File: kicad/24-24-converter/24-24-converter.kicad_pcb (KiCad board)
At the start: 4 copper layers, 143.5 x 76 mm, 79 parts, among them J1 Conn_01x02, J2 Conn_01x02, M1 CSD18540Q5B, M1_1 CSD18540Q5B, M2 CSD18540Q5B, M2_1 CSD18540Q5B, M3 GENERIC_MOSFET_N, M3_1 GENERIC_MOSFET_N, M4 GENERIC_MOSFET_N, U1 LM5176PWPR

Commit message: Routing Attempt #2
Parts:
- moved Ccomp2 10.6 mm to (132.0, 107.5), turned to -90 degrees
- moved Ccomp1 8.01 mm to (129.5, 107.5), turned to -90 degrees
- moved Rpg1 6.18 mm to (162.0, 102.5)
- moved D2 5.70 mm to (159.5, 102.0), turned to 90 degrees
- moved Cvcc1 5.41 mm to (164.5, 102.5)
- moved Rcsp1 5.22 mm to (156.5, 101.0)
- moved Ccomp_1 3.96 mm to (133.5, 112.0), turned to -90 degrees
- moved Ccs1 3.54 mm to (153.5, 101.0), turned to 90 degrees
- moved Css1 3.51 mm to (135.0, 107.5)
- moved Rcsg1 2.69 mm to (150.0, 101.0)
- moved Rcomp1 2.64 mm to (129.5, 112.0)
- moved Dboot2 1.22 mm to (158.7, 106.0)
- moved Dboot1 0.97 mm to (155.0, 109.5)
- moved Cboot2 0.50 mm to (153.5, 106.0)
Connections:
- M3 pad 9: (no net) -> VOUT
- M3_1 pad 9: (no net) -> VOUT
- M4 pad 9: (no net) -> /SW2
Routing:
- net GND: track 449.2 -> 361.8 mm, vias 177 -> 18
- net Net-(U1-COMP): track 33.9 -> 17.2 mm
- net Net-(Dboot1-A): track 29.9 -> 19.9 mm
- net VOUT: track 241.1 -> 234.1 mm, vias 56 -> 3
- net /CSENSE: track 55.7 -> 61.4 mm
- net Net-(D2-A): track 7.41 -> 2.95 mm
- net Net-(D2-K): track 15.9 -> 11.9 mm
- net Net-(U1-CS): track 13.2 -> 9.29 mm
- net /HDRV1: track 60.6 -> 64.5 mm
- net Net-(U1-SS): track 10.7 -> 7.02 mm
- net /LDRV2: track 40.1 -> 37.6 mm
- net Net-(U1-CSG): track 5.07 -> 6.83 mm
- net Net-(Ccomp1-Pad2): track 5.80 -> 7.34 mm
- net /SW1: track 130.0 -> 130.8 mm, vias 54 -> 3
- net /HDRV2: track 64.9 -> 64.3 mm
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- added copper zone on F.Cu, net /CSENSE
- removed copper zone on In1.Cu, net /SW1
- removed copper zone on In1.Cu, net /SW2
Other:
- board text added: "Routing Attempt #2"
- board text removed: "Routing Attempt #1"

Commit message: All new routing around U1
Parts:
- moved D3 11.0 mm to (200.0, 56.5)
- moved R2 11.0 mm to (194.0, 56.5)
- moved Css1 3.03 mm to (137.9, 106.5), turned to 180 degrees
- moved Dboot1 2.00 mm to (157.0, 109.5)
- moved Cvcc1 0.50 mm to (164.0, 102.5)
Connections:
- M3 pad 9: VOUT -> (no net)
- M3_1 pad 9: VOUT -> (no net)
- M4 pad 9: /SW2 -> (no net)
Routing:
- net VOUT: track 234.1 -> 186.5 mm
- net Net-(U1-VIN): track 38.9 -> 55.1 mm, vias 2 -> 4
- net /HDRV2: track 64.3 -> 53.7 mm, vias 5 -> 3
- net Net-(U1-BIAS): track 12.6 -> 22.9 mm
- net GND: track 361.8 -> 352.6 mm
- net /HDRV1: track 64.5 -> 70.0 mm
- net /LDRV1: track 50.6 -> 55.6 mm
- net Net-(U1-SS): track 7.02 -> 3.14 mm
- net /SW2: track 116.1 -> 119.2 mm
- net /EN: track 26.3 -> 28.5 mm, vias 2 -> 4
- net /SW1: track 130.8 -> 128.8 mm
- net Net-(Dboot1-K): track 8.91 -> 10.9 mm
- net Net-(U1-VINSNS): track 33.1 -> 32.4 mm, vias 2 -> 4

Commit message: Added Watermark
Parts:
- added G***: LOGO, LOGO, F.Cu at (191.5, 122.0)

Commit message: Routing Attempt #3
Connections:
- M3 pad 9: (no net) -> VOUT
- M3_1 pad 9: (no net) -> VOUT
- M4 pad 9: (no net) -> /SW2
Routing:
- net GND: track 352.6 -> 38.7 mm, vias 18 -> 593
- net VIN: track 200.7 -> 37.8 mm, vias 1 -> 197
- net VOUT: track 186.5 -> 56.2 mm, vias 3 -> 58
- net /SW1: track 128.8 -> 55.7 mm, vias 3 -> 75
- net /SW2: track 119.2 -> 49.7 mm, vias 3 -> 71
- net /CSENSE: track 61.4 -> 23.3 mm, vias 1 -> 17
- net /LDRV1: track 55.6 -> 60.1 mm, vias 3 -> 4
- added copper zone on B.Cu, net /CSENSE
- added copper zone on B.Cu, net /SW1
- added copper zone on B.Cu, net /SW2
- added copper zone on B.Cu, net VIN
- added copper zone on B.Cu, net VOUT
- removed copper zone on In1.Cu, net VIN
- removed copper zone on In1.Cu, net VOUT
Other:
- board text added: "Routing Attempt #3"
- board text removed: "Routing Attempt #2"

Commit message: Routing Attempt #4
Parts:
- U1: value LM5176PWPR -> PWP0028C_N
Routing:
- net GND: vias 593 -> 614
- net /SW1: vias 75 -> 77
- net /LDRV2: vias 3 -> 4
- net /LDRV1: vias 4 -> 5
- net /CSENSE: vias 17 -> 26
- removed copper zone on F.Cu, net (none)
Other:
- board text added: "Routing Attempt #4"
- board text removed: "Routing Attempt #3"

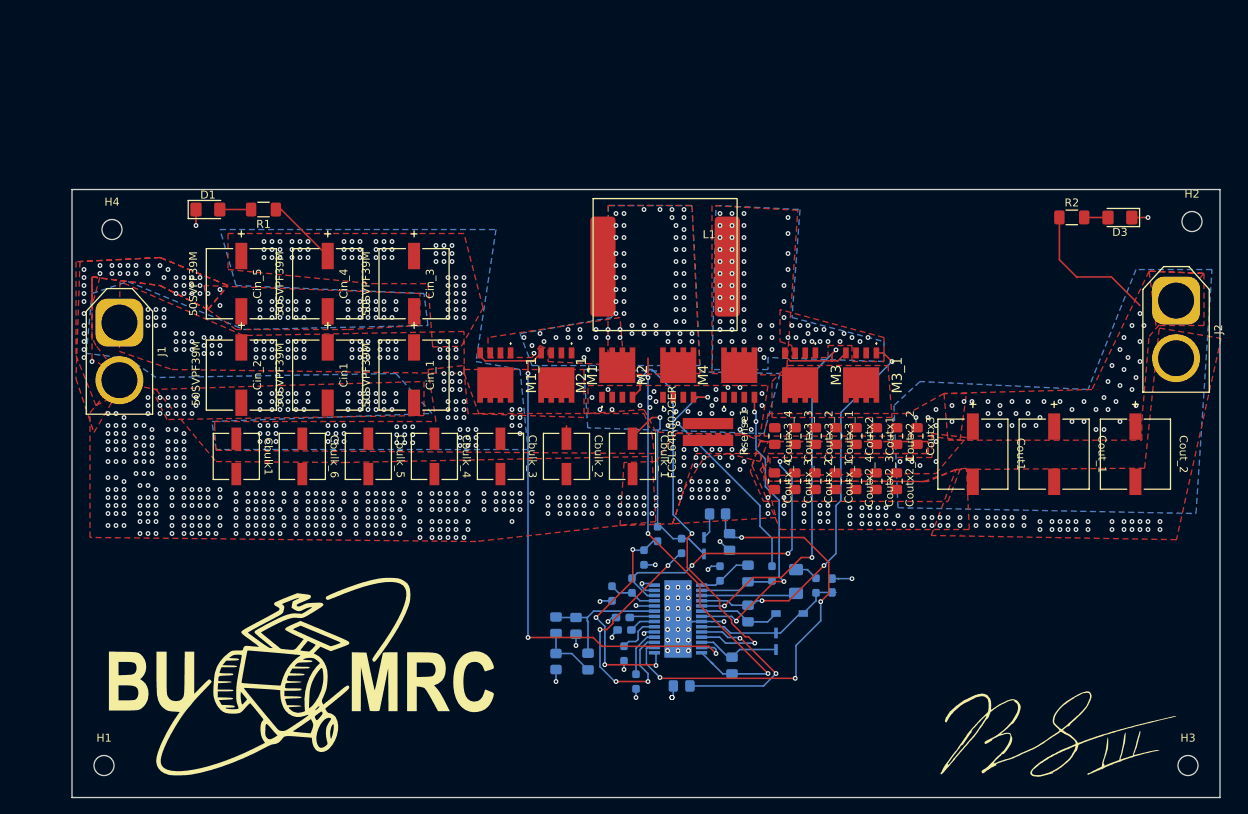
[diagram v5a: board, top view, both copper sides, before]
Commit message: Resolved DRC Flags
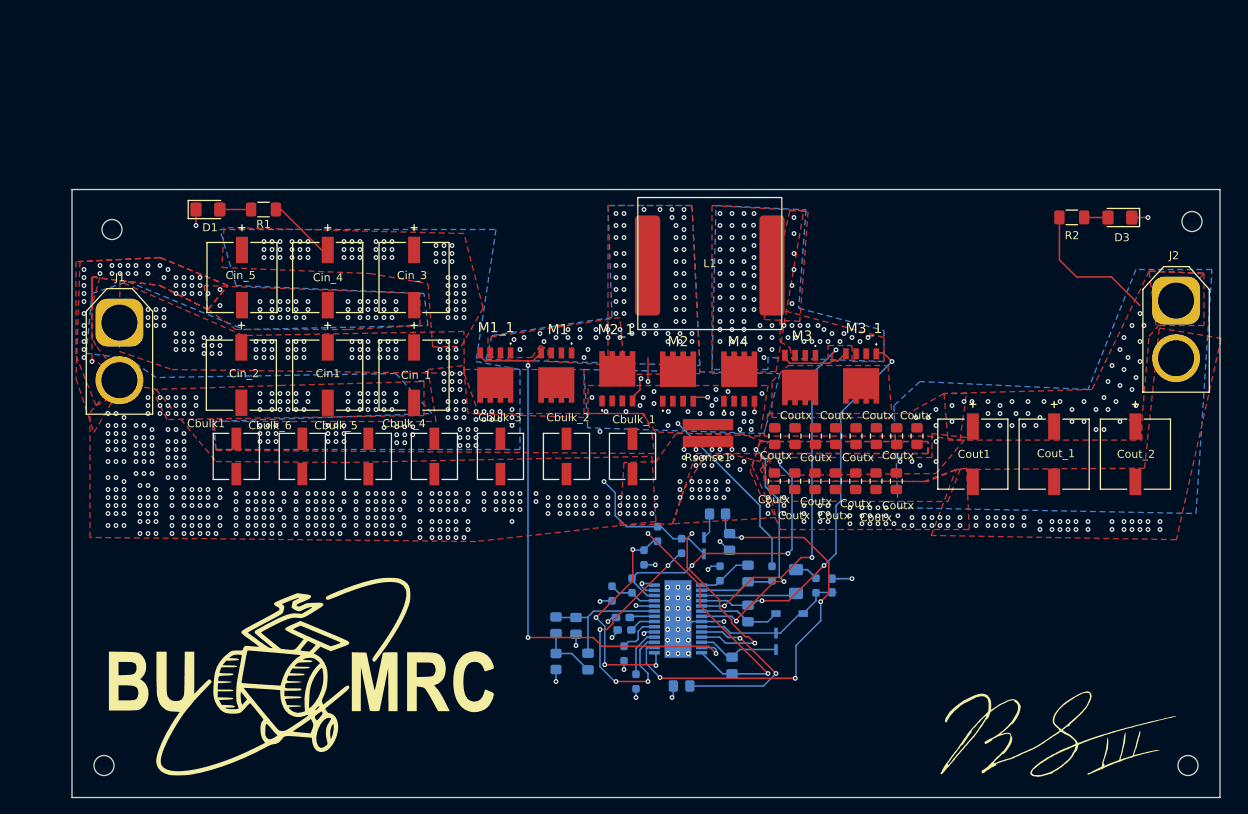
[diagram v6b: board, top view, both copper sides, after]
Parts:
- moved L1 5.59 mm to (148.7, 62.5)
- moved Cin_5 0.77 mm to (90.2, 64.0)
- moved Cin_3 0.77 mm to (111.8, 64.0)
- moved Cin_4 0.77 mm to (101.0, 64.0)
- moved M2 0.50 mm to (144.8, 76.7)
- moved M4 0.49 mm to (152.4, 76.7)
- moved M2_1 0.46 mm to (137.2, 76.7)
- moved M3 0.30 mm to (160.0, 76.5)
- moved Rsense1 0.14 mm to (148.5, 83.4)
- moved M3_1 0.11 mm to (167.6, 76.3)
- renumbered Coutx_1 to Coutx, Coutx2_1 to Coutx, Coutx2 to Coutx, Coutx_3 to Coutx, Coutx3_1 to Coutx, Coutx2_4 to Coutx, Coutx3_2 to Coutx, Coutx3 to Coutx, Coutx3_4 to Coutx, Coutx_2 to Coutx, Coutx2_2 to Coutx, Coutx_4 to Coutx, Coutx2_3 to Coutx, Coutx1 to Coutx, Coutx3_3 to Coutx
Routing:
- net VIN: track 37.8 -> 34.3 mm, vias 197 -> 202
- net /LDRV1: track 60.1 -> 58.2 mm, vias 5 -> 4
- net /SW1: track 55.7 -> 56.7 mm, vias 77 -> 75
- net /SW2: track 49.7 -> 49.3 mm, vias 71 -> 80
- net GND: vias 614 -> 612
- net /CSENSE: vias 26 -> 25
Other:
- board text removed: "Routing Attempt #4"

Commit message: Routing Attempt #5
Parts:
- removed Cbulk1, Cbulk_1, Cbulk_2, Cbulk_3, Cbulk_4, Cbulk_5, Cbulk_6: 50SVPF10M, 24V_Converter:Cbulk_CAP_B6-SVPK_PAN
- removed Ccomp1, Ccomp_1: MSASH21GSB7153MTNA01, Capacitor_SMD:C_0805_2012Metric_Pad1.18x1.45mm_HandSolder
- removed Ccomp2: GRM2195C1H152JA01D, Capacitor_SMD:C_0805_2012Metric_Pad1.18x1.45mm_HandSolder
- removed Cin1, Cin_1, Cin_2, Cin_3, Cin_4, Cin_5: 50SVPF39M, 24V_Converter:Cin_50SVPF39M
- removed Cout1, Cout_1, Cout_2: 35SVPF82M, 24V_Converter:PCAP_SVP_E12_PAN
- removed Coutx (x15): MSASU21GBB5475KTNA01, Capacitor_SMD:C_0805_2012Metric_Pad1.18x1.45mm_HandSolder
- added C1: 50SVPF10M, 24V_Converter:Cbulk_CAP_B6-SVPK_PAN, F.Cu at (139.0, 86.0)
- added C10: MSASU21GBB5475KTNA01, Capacitor_SMD:C_0805_2012Metric_Pad1.18x1.45mm_HandSolder, F.Cu at (169.2, 88.8)
- added C11: MSASU21GBB5475KTNA01, Capacitor_SMD:C_0805_2012Metric_Pad1.18x1.45mm_HandSolder, F.Cu at (166.0, 89.0)
- added C12: MSASU21GBB5475KTNA01, Capacitor_SMD:C_0805_2012Metric_Pad1.18x1.45mm_HandSolder, F.Cu at (163.0, 89.0)
- added C13: 50SVPF39M, 24V_Converter:Cin_50SVPF39M, F.Cu at (90.5, 63.9)
- added C14: 50SVPF39M, 24V_Converter:Cin_50SVPF39M, F.Cu at (101.0, 64.2)
- added C15: 50SVPF39M, 24V_Converter:Cin_50SVPF39M, F.Cu at (112.2, 64.2)
- added C16: 50SVPF39M, 24V_Converter:Cin_50SVPF39M, F.Cu at (89.5, 76.4)
- added C17: 50SVPF39M, 24V_Converter:Cin_50SVPF39M, F.Cu at (100.5, 76.4)
- added C18: 50SVPF39M, 24V_Converter:Cin_50SVPF39M, F.Cu at (111.8, 76.2)
- added C19: MSASU21GBB5475KTNA01, Capacitor_SMD:C_0805_2012Metric_Pad1.18x1.45mm_HandSolder, F.Cu at (160.5, 88.8)
- added C2: 50SVPF10M, 24V_Converter:Cbulk_CAP_B6-SVPK_PAN, F.Cu at (130.8, 86.2)
- added C20: MSASU21GBB5475KTNA01, Capacitor_SMD:C_0805_2012Metric_Pad1.18x1.45mm_HandSolder, F.Cu at (158.0, 88.8)
- added C21: MSASU21GBB5475KTNA01, Capacitor_SMD:C_0805_2012Metric_Pad1.18x1.45mm_HandSolder, F.Cu at (174.0, 83.5)
- added C22: MSASU21GBB5475KTNA01, Capacitor_SMD:C_0805_2012Metric_Pad1.18x1.45mm_HandSolder, F.Cu at (171.5, 83.5)
- added C23: MSASU21GBB5475KTNA01, Capacitor_SMD:C_0805_2012Metric_Pad1.18x1.45mm_HandSolder, F.Cu at (169.0, 83.5)
- added C24: MSASU21GBB5475KTNA01, Capacitor_SMD:C_0805_2012Metric_Pad1.18x1.45mm_HandSolder, F.Cu at (166.8, 83.5)
- added C25: MSASU21GBB5475KTNA01, Capacitor_SMD:C_0805_2012Metric_Pad1.18x1.45mm_HandSolder, F.Cu at (164.5, 83.5)
- added C26: MSASU21GBB5475KTNA01, Capacitor_SMD:C_0805_2012Metric_Pad1.18x1.45mm_HandSolder, F.Cu at (162.0, 83.6)
- added C27: MSASU21GBB5475KTNA01, Capacitor_SMD:C_0805_2012Metric_Pad1.18x1.45mm_HandSolder, F.Cu at (159.5, 83.6)
- added C28: MSASU21GBB5475KTNA01, Capacitor_SMD:C_0805_2012Metric_Pad1.18x1.45mm_HandSolder, F.Cu at (157.0, 83.6)
- added C29: 35SVPF82M, 24V_Converter:PCAP_SVP_E12_PAN, F.Cu at (181.8, 86.3)
- added C3: 50SVPF10M, 24V_Converter:Cbulk_CAP_B6-SVPK_PAN, F.Cu at (122.8, 86.2)
- added C30: 35SVPF82M, 24V_Converter:PCAP_SVP_E12_PAN, F.Cu at (192.0, 86.8)
- added C31: 35SVPF82M, 24V_Converter:PCAP_SVP_E12_PAN, F.Cu at (201.8, 86.8)
- added C32: MSASH21GSB7153MTNA01, Capacitor_SMD:C_0805_2012Metric_Pad1.18x1.45mm_HandSolder, B.Cu at (138.2, 104.8)
- added C33: MSASH21GSB7153MTNA01, Capacitor_SMD:C_0805_2012Metric_Pad1.18x1.45mm_HandSolder, B.Cu at (138.2, 102.8)
- added C34: GRM2195C1H152JA01D, Capacitor_SMD:C_0805_2012Metric_Pad1.18x1.45mm_HandSolder, B.Cu at (138.5, 100.5)
- added C4: 50SVPF10M, 24V_Converter:Cbulk_CAP_B6-SVPK_PAN, F.Cu at (114.5, 86.2)
- added C5: 50SVPF10M, 24V_Converter:Cbulk_CAP_B6-SVPK_PAN, F.Cu at (106.0, 86.2)
- added C6: 50SVPF10M, 24V_Converter:Cbulk_CAP_B6-SVPK_PAN, F.Cu at (97.8, 86.2)
- added C7: 50SVPF10M, 24V_Converter:Cbulk_CAP_B6-SVPK_PAN, F.Cu at (89.6, 86.2)
- added C8: MSASU21GBB5475KTNA01, Capacitor_SMD:C_0805_2012Metric_Pad1.18x1.45mm_HandSolder, F.Cu at (175.8, 88.8)
- added C9: MSASU21GBB5475KTNA01, Capacitor_SMD:C_0805_2012Metric_Pad1.18x1.45mm_HandSolder, F.Cu at (172.5, 88.8)
- added J3: Enable, Connector_AMASS:AMASS_XT30U-M_1x02_P5.0mm_Vertical, F.Cu at (143.8, 124.5)
- U1: value PWP0028C_N -> LM5176PWPR
- moved Cvcc1 15.6 mm to (152.5, 113.0), turned to -90 degrees
- moved Rcomp1 12.4 mm to (134.2, 100.5), turned to 180 degrees
- moved Cbias1 9.49 mm to (151.2, 107.8), turned to 0 degrees
- moved Rfbb1 5.27 mm to (131.2, 104.0), turned to 180 degrees
- moved Cf1 5.08 mm to (156.2, 96.5), turned to 0 degrees
- moved Rfbt1 5.06 mm to (134.0, 103.2)
- moved Rf1 4.57 mm to (150.8, 98.0)
- moved Rpg1 4.33 mm to (160.0, 106.3)
- moved D2 4.03 mm to (156.0, 104.0), turned to 0 degrees
- moved Rmode1 3.72 mm to (138.2, 111.0), turned to 180 degrees
- moved Dboot1 3.34 mm to (153.8, 110.2), turned to 0 degrees
- moved Ruvb1 3.18 mm to (138.2, 96.8), turned to 180 degrees
- moved Ccs1 3.02 mm to (150.8, 102.2), turned to 180 degrees
- moved Dboot2 2.75 mm to (156.2, 107.2)
- moved Cboot2 2.06 mm to (151.5, 105.5), turned to 0 degrees
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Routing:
- net Net-(U1-VIN): track 55.1 -> 27.0 mm, vias 4 -> 2
- net Net-(U1-BIAS): track 22.9 -> 2.88 mm, vias 2 -> 0
- net Net-(U1-VINSNS): track 32.4 -> 20.3 mm, vias 4 -> 2
- net /SW1: track 56.7 -> 46.2 mm
- net Net-(U1-COMP): track 17.3 -> 7.26 mm
- net /EN: track 28.5 -> 37.8 mm, vias 4 -> 2
- net /LDRV1: track 58.2 -> 50.3 mm, vias 4 -> 5
- net /SW2: track 49.3 -> 43.1 mm
- net VOUT: track 56.1 -> 50.1 mm, vias 58 -> 88
- net GND: track 38.7 -> 33.4 mm, vias 612 -> 638
- net Net-(Dboot1-K): track 10.9 -> 5.79 mm
- net Net-(D2-K): track 11.9 -> 6.91 mm
- net /CSENSE: track 23.3 -> 18.9 mm
- net /LDRV2: track 37.3 -> 33.3 mm
- net Net-(U1-FB): track 6.30 -> 10.3 mm, vias 0 -> 2
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
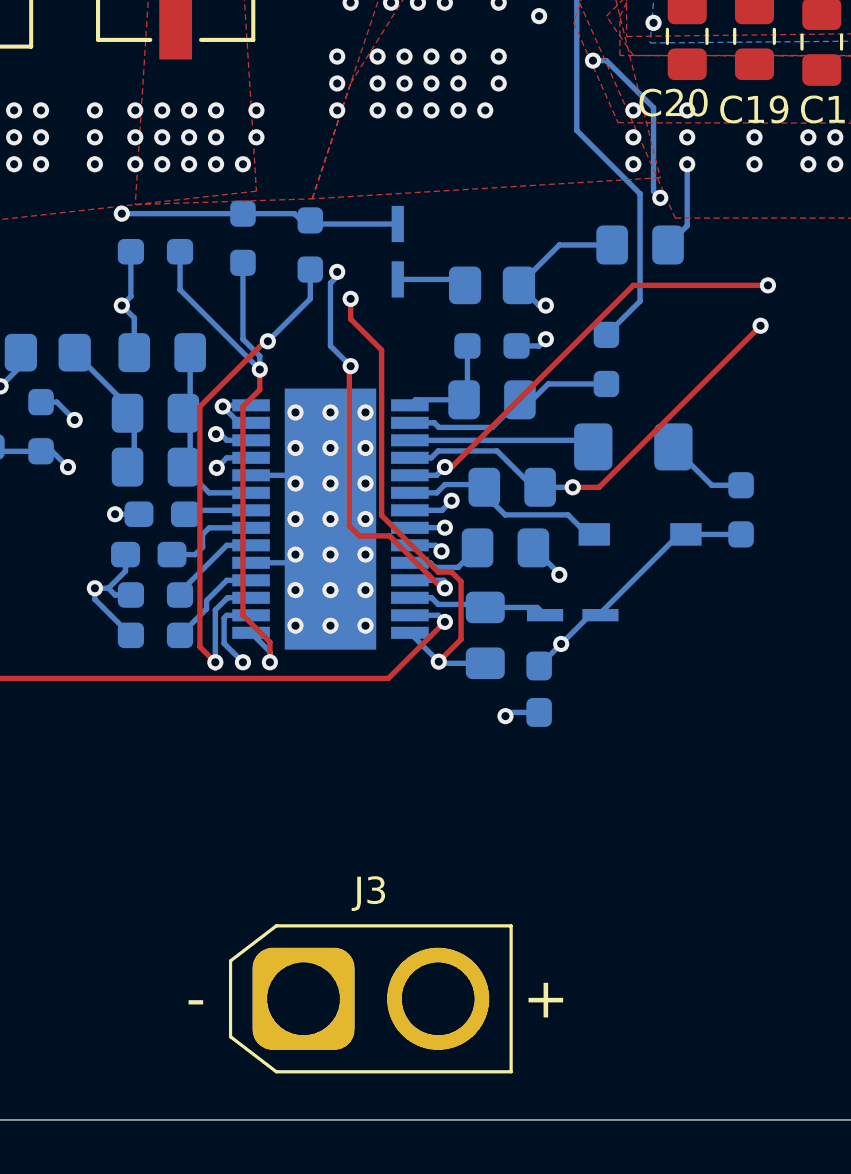
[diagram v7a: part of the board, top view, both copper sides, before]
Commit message: Fixed Capacitor
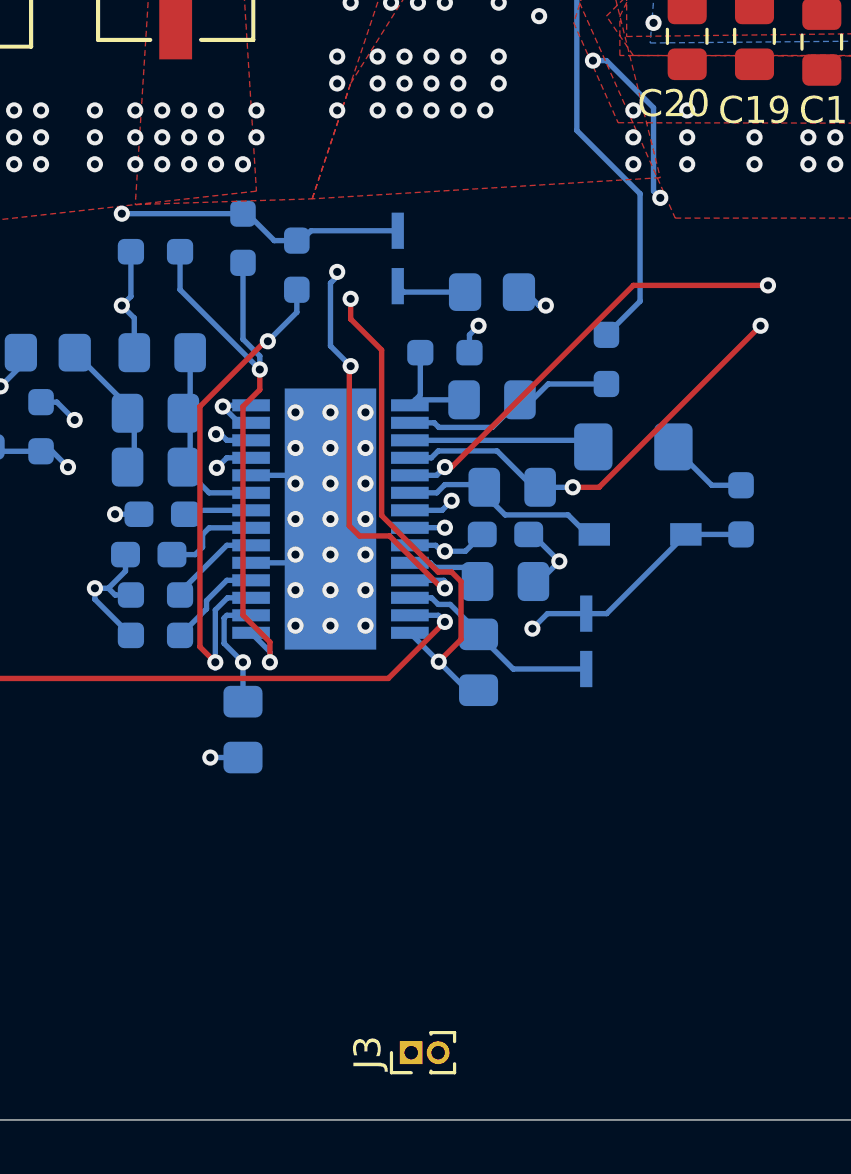
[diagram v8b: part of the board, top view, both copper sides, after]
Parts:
- J3: footprint Connector_AMASS:AMASS_XT30U-M_1x02_P5.0mm_Vertical -> Connector_PinHeader_1.00mm:PinHeader_1x02_P1.00mm_Vertical
- moved Cf1 23.3 mm to (141.5, 114.5), turned to -90 degrees
- moved Cvcc1 5.88 mm to (151.2, 107.2), turned to 0 degrees
- moved J3 4.47 mm to (147.8, 126.5), turned to 90 degrees
- moved Rcsg1 1.77 mm to (149.0, 100.5)
- moved Cbias1 1.25 mm to (151.2, 109.0)
- moved Dboot1 1.09 mm to (154.2, 111.2), turned to 90 degrees
- moved Cboot1 1.03 mm to (150.2, 112.0)
- moved Rvisns1 0.90 mm to (143.5, 97.2)
- moved Df1 0.25 mm to (147.2, 97.0)
- moved Rf1 0.25 mm to (150.8, 98.2)
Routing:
- net Net-(U1-VIN): track 27.0 -> 24.4 mm
- net GND: track 33.4 -> 31.3 mm
- net /EN: track 37.8 -> 39.8 mm
- net Net-(Dboot1-K): track 5.79 -> 7.68 mm
- net Net-(U1-VINSNS): track 20.3 -> 19.3 mm
- net Net-(Dboot1-A): track 16.6 -> 17.3 mm
